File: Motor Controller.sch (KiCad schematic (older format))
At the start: 18 parts, among them U10 2X3Header, U2 TC4427, U4 TC4427, U7 ZXMHC3F381N8, U8 ZXMHC3F381N8, U9 2X3Header

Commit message: removed SD Card
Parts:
- U7, U8: footprint Housings_SOIC:Diodes_PSOP-8 -> micromouse:ZXMHC3F381N8
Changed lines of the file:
@@
 F 0 "U7" H 5000 2450 60  0000 L CNN
 F 1 "ZXMHC3F381N8" H 5000 2350 60  0000 L CNN
-F 2 "Housings_SOIC:Diodes_PSOP-8" H 4800 2200 60  0001 C CNN
+F 2 "micromouse:ZXMHC3F381N8" H 4800 2200 60  0001 C CNN
 F 3 "" H 4800 2200 60  0001 C CNN
 	1    4800 2200
@@
 F 0 "U8" H 5100 5325 60  0000 L CNN
 F 1 "ZXMHC3F381N8" H 5100 5225 60  0000 L CNN
-F 2 "Housings_SOIC:Diodes_PSOP-8" H 4900 5075 60  0001 C CNN
+F 2 "micromouse:ZXMHC3F381N8" H 4900 5075 60  0001 C CNN
 F 3 "" H 4900 5075 60  0001 C CNN
 	1    4900 5075

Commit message: generated a netlist
filled the teensy components with 0402 size untill i find out more info.
Starting to do PCB layout.
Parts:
- U2, U4: footprint sop:MSOP8 -> micromouse:TC4427_MSOP8
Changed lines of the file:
@@
 F 0 "U2" H 2700 2450 60  0000 L CNN
 F 1 "TC4427" H 2700 2350 60  0000 L CNN
-F 2 "sop:MSOP8" H 2500 2200 60  0001 C CNN
+F 2 "micromouse:TC4427_MSOP8" H 2500 2200 60  0001 C CNN
 F 3 "" H 2500 2200 60  0001 C CNN
 	1    2500 2200
@@
 F 0 "U4" H 2800 5325 60  0000 L CNN
 F 1 "TC4427" H 2800 5225 60  0000 L CNN
-F 2 "sop:MSOP8" H 2600 5075 60  0001 C CNN
+F 2 "micromouse:TC4427_MSOP8" H 2600 5075 60  0001 C CNN
 F 3 "" H 2600 5075 60  0001 C CNN
 	1    2600 5075

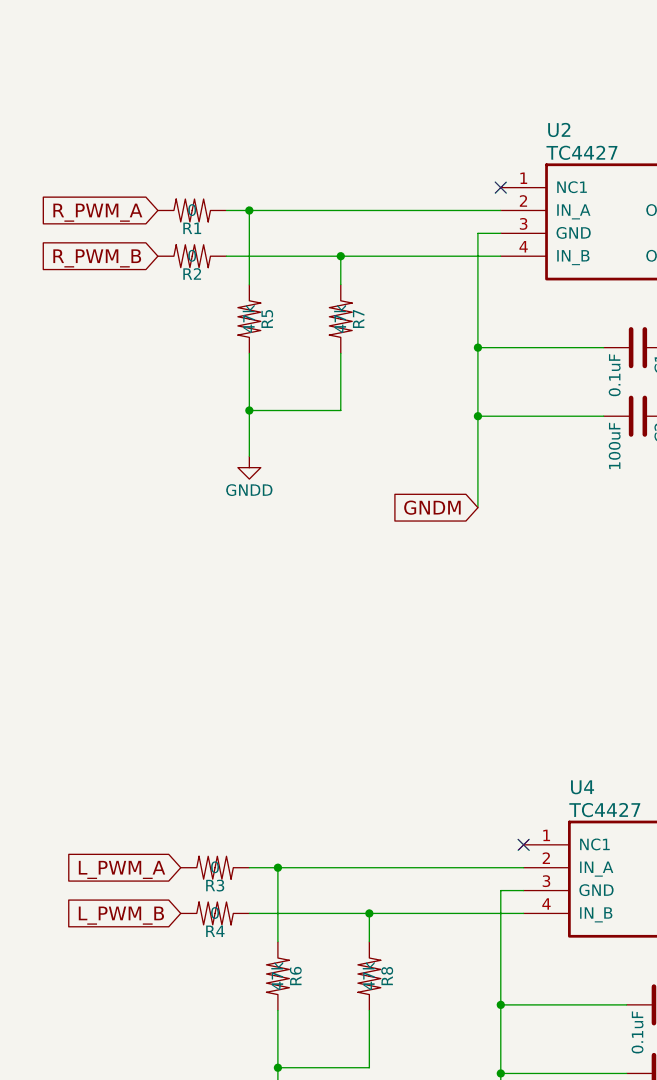
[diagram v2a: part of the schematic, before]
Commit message: Added MPU-6500
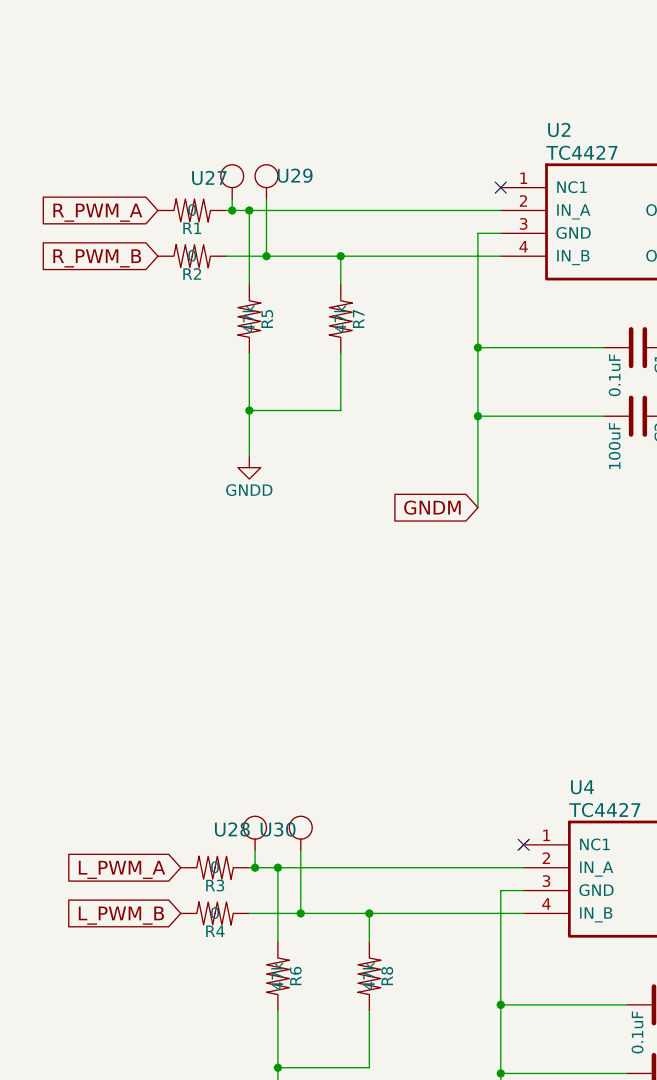
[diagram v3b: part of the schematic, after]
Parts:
- added U27, U28, U29, U30: Test_Point, micromouse:Test_Point, symbol Test_Point
- U10, U9: footprint Socket_Strips:Socket_Strip_Straight_2x03_Pitch2.54mm -> micromouse:Motors_connectors
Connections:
- net at R1.1, R5.1, U2.2 (IN_A): now also U27.1
- net at R2.1, R7.1, U2.4 (IN_B): now also U29.1
- net at R3.1, R6.1, U4.2 (IN_A): now also U28.1
- net at R4.1, R8.1, U4.4 (IN_B): now also U30.1

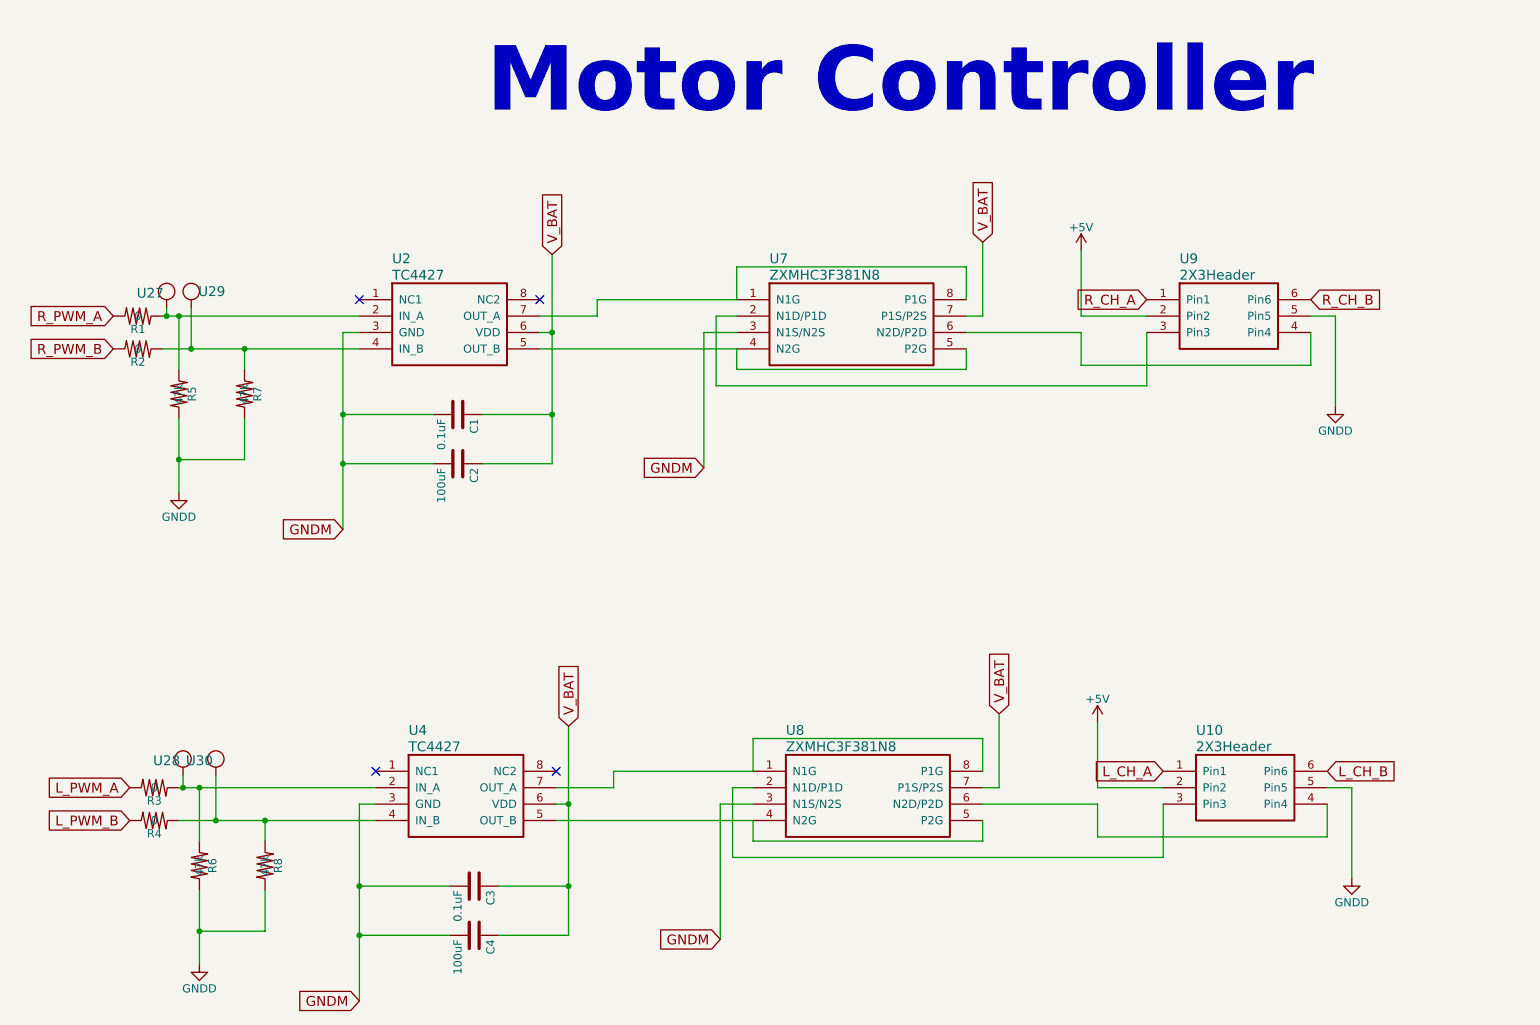
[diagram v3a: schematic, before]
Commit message: finished floor planning
-replaced the TC4427 and H brige by a single DRV8833 chip
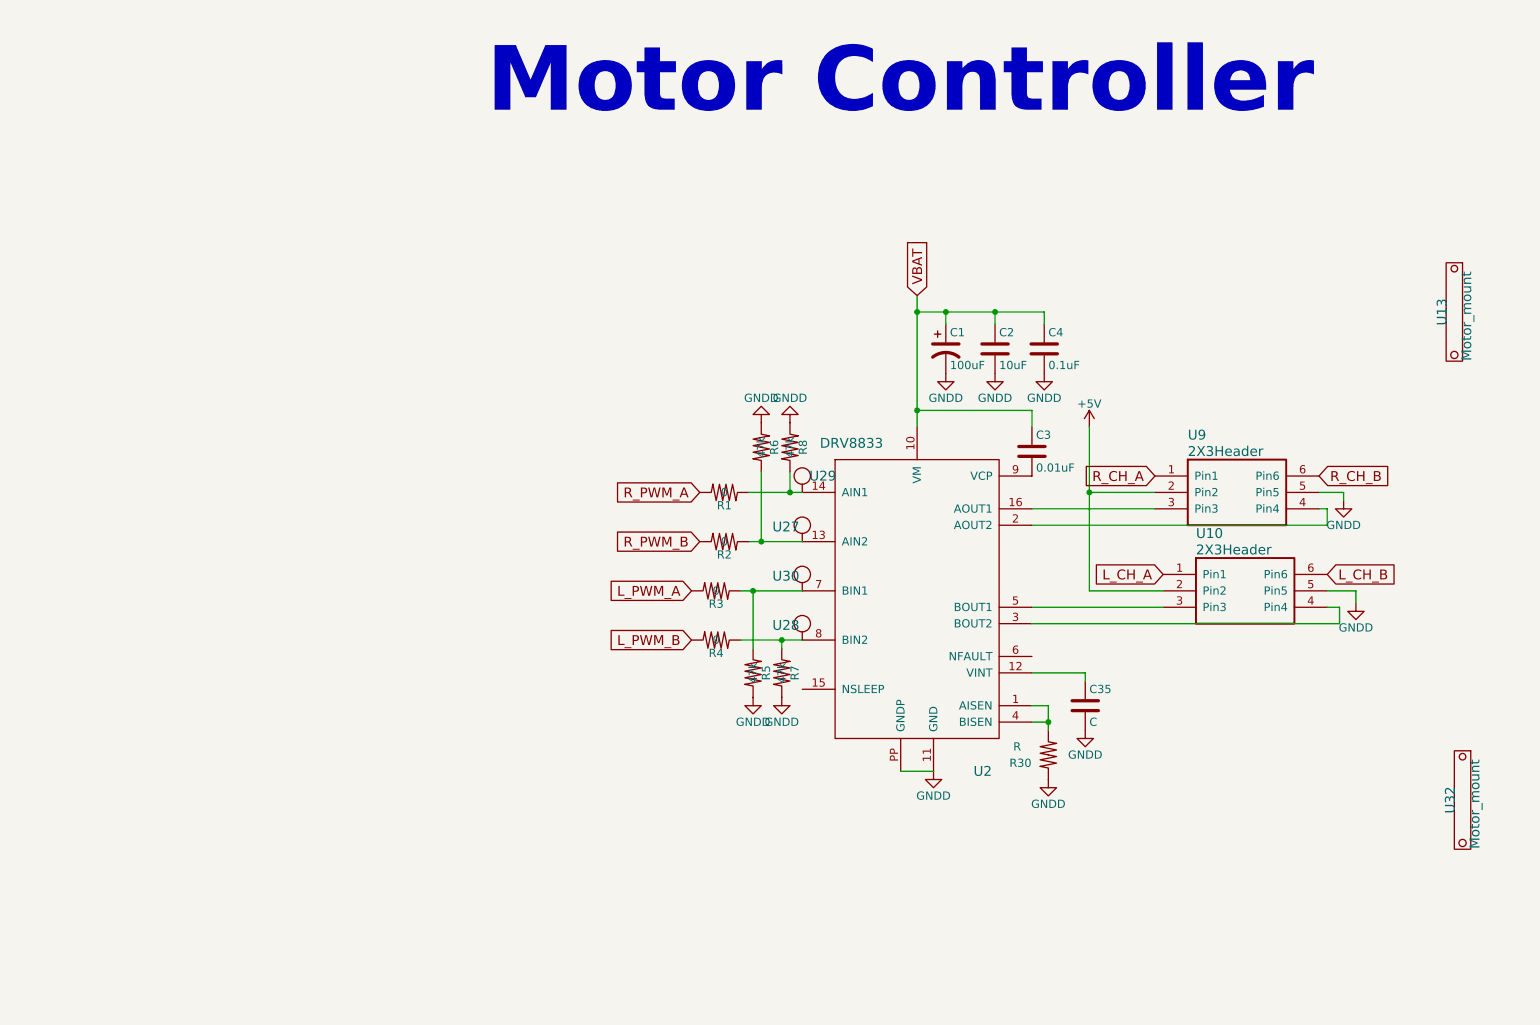
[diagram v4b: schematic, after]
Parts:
- removed C1: 0.1uF, Capacitors_SMD:C_0603, symbol C
- removed U2, U4: TC4427, micromouse:TC4427_MSOP8, symbol TC4427
- removed U7, U8: ZXMHC3F381N8, micromouse:ZXMHC3F381N8, symbol ZXMHC3F381N8
- added C1: 100uF, symbol CP1
- added C35: C, Capacitors_SMD:C_0402, symbol C
- added R30: R, symbol R
- added U13, U32: Motor_mount, micromouse:Motor_mount, symbol Motor_mount
- added U2: DRV8833, micromouse:DRV8833, symbol DRV8833
- C2: value 100uF -> 10uF; footprint Capacitors_SMD:C_0603 -> Capacitors_SMD:C_0805; manf# (none) -> C2012X5R1C106M
- C3: value 0.1uF -> 0.01uF; footprint Capacitors_SMD:C_0603 -> (none); manf# (none) -> GRM188R71E103KA01D
- C4: value 100uF -> 0.1uF; manf# (none) -> C1608X7R1E104K
- R1, R2, R3, R4, R5, R6, R7, R8: footprint Resistors_SMD:R_0603 -> Capacitors_SMD:C_0402
- U10, U9: manf# (none) -> M20-9980345
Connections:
- net GNDD: now also C2.2, C4.2, R6.1, R8.1, C1.2, C35.2, R30.2, U2.11 (GND), U2.PP (GNDP); no longer R6.2, R8.2
- net at U9.3 (Pin3): now also U2.16 (AOUT1)
- net at U9.4 (Pin4): now also U2.2 (AOUT2)
- net at U10.3 (Pin3): now also U2.5 (BOUT1)
- net at U10.4 (Pin4): now also U2.3 (BOUT2)
- removed net GNDM: C2.2, C3.2, C4.2
- net V_BAT renamed VBAT
- net VBAT: now also C1.1, U2.10 (VM)
- new net: R1.1, R8.2, U2.14 (AIN1), U29.1
- new net: R2.1, R6.2, U2.13 (AIN2), U27.1
- new net: R3.1, R5.1, U2.7 (BIN1), U30.1
- new net: R4.1, R7.1, U2.8 (BIN2), U28.1
- new net: R30.1, U2.1 (AISEN), U2.4 (BISEN)
- new net: C35.1, U2.12 (VINT)
- new net: C3.2, U2.9 (VCP)
- no-connect marks 4 -> 0
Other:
- moved on the sheet: R1, R2, R3, R4, R8, U10, U27, U28, U29, U30, U9
